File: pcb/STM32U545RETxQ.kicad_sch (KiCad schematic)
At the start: 20 parts, among them U3 STM32U545RETxQ

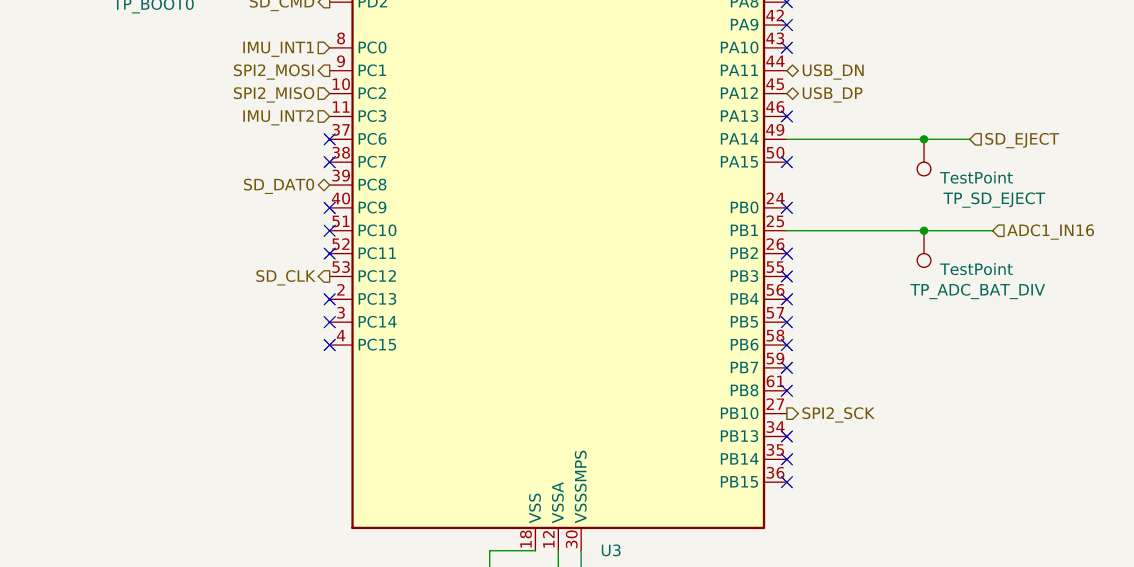
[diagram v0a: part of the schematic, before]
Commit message: Updated Control Mod test bed schematics
finished testpoints, got rid of Vbus and replaced with +5V, added +3.3v to pyro J1 terminal
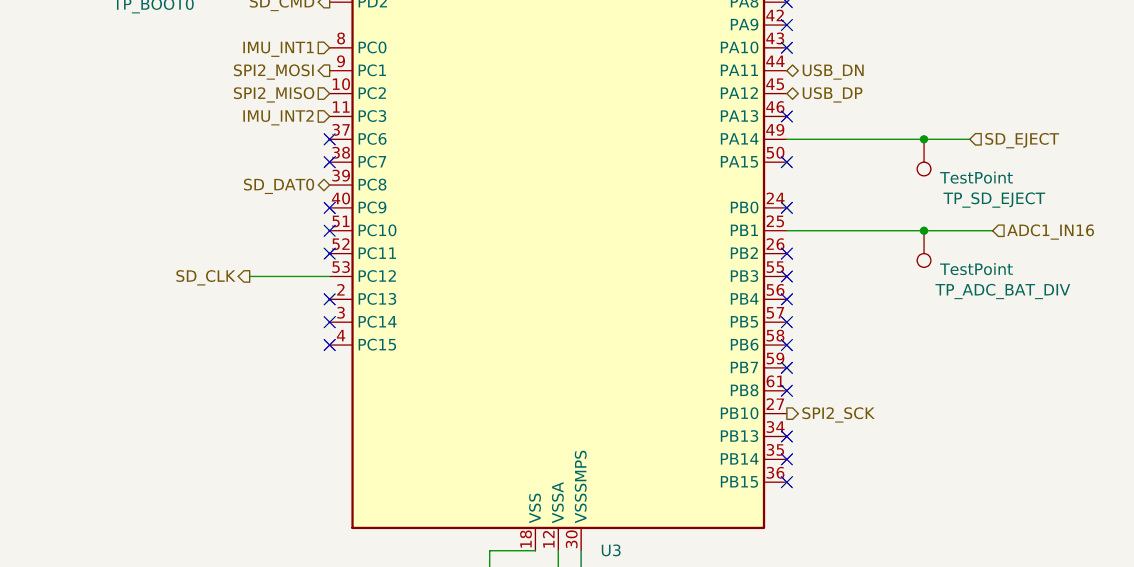
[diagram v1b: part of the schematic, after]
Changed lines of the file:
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@@
+	(wire
+		(pts
+			(xy 124.46 109.22) (xy 133.35 109.22)
+		)
+		(stroke
+			(width 0)
+			(type default)
+		)
+	)
 	(wire
 		(pts
@@
 	(hierarchical_label "SD_CLK"
 		(shape output)
-		(at 133.35 109.22 180)
+		(at 124.46 109.22 180)
 		(effects
 			(font
@@
 		(dnp no)
 		(property "Reference" "TP_ADC_BAT_DIV"
-			(at 212.852 110.744 0)
-			(effects
-				(font
+			(at 215.646 110.744 0)
+			(effects
+				(font
